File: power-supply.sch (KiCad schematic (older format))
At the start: 18 parts

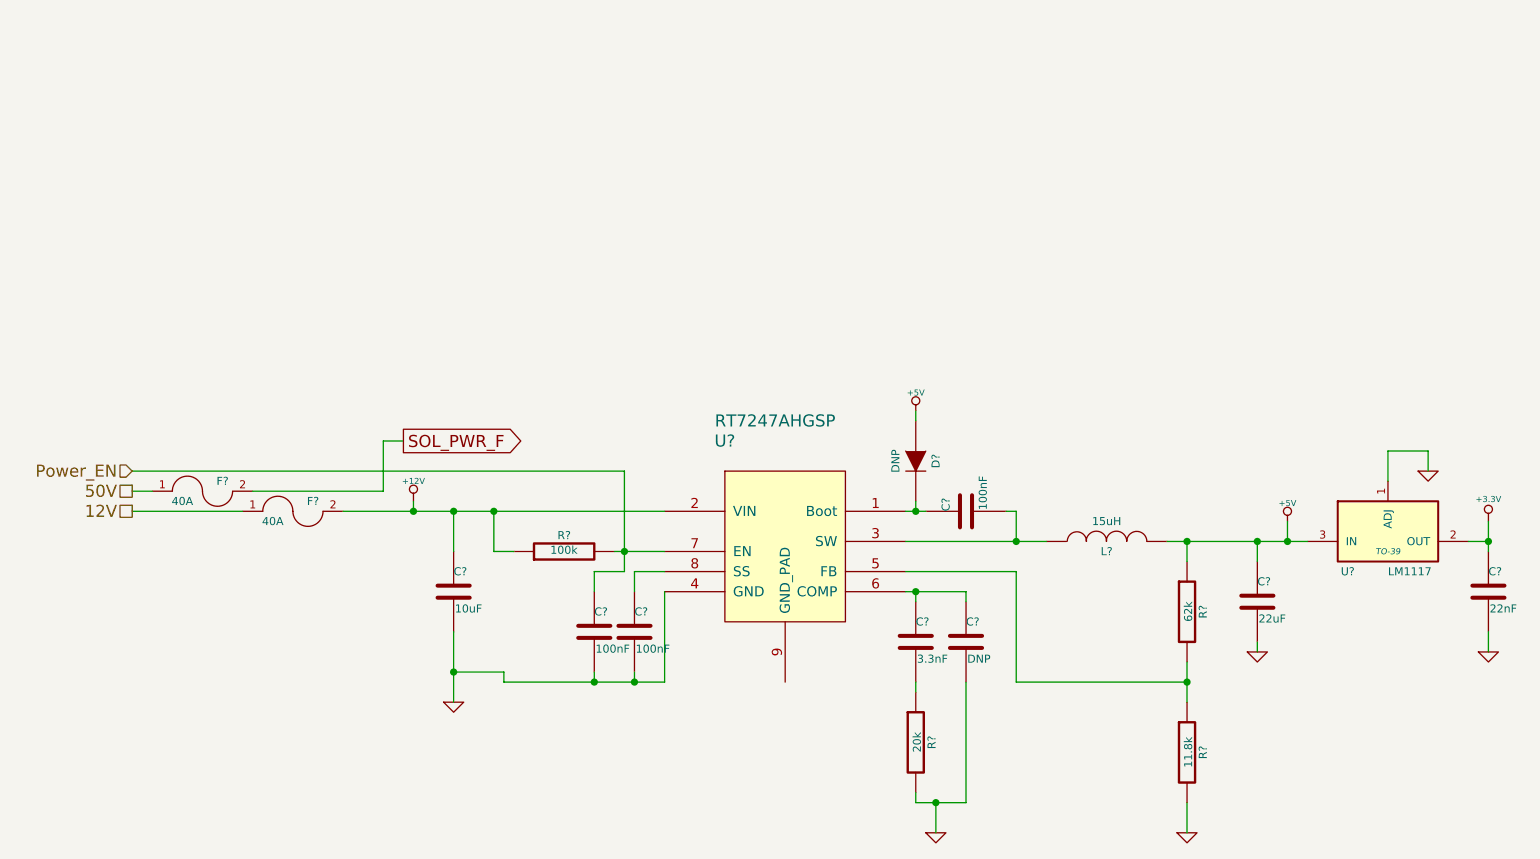
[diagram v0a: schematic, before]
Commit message: changed the controller adding some shift registers
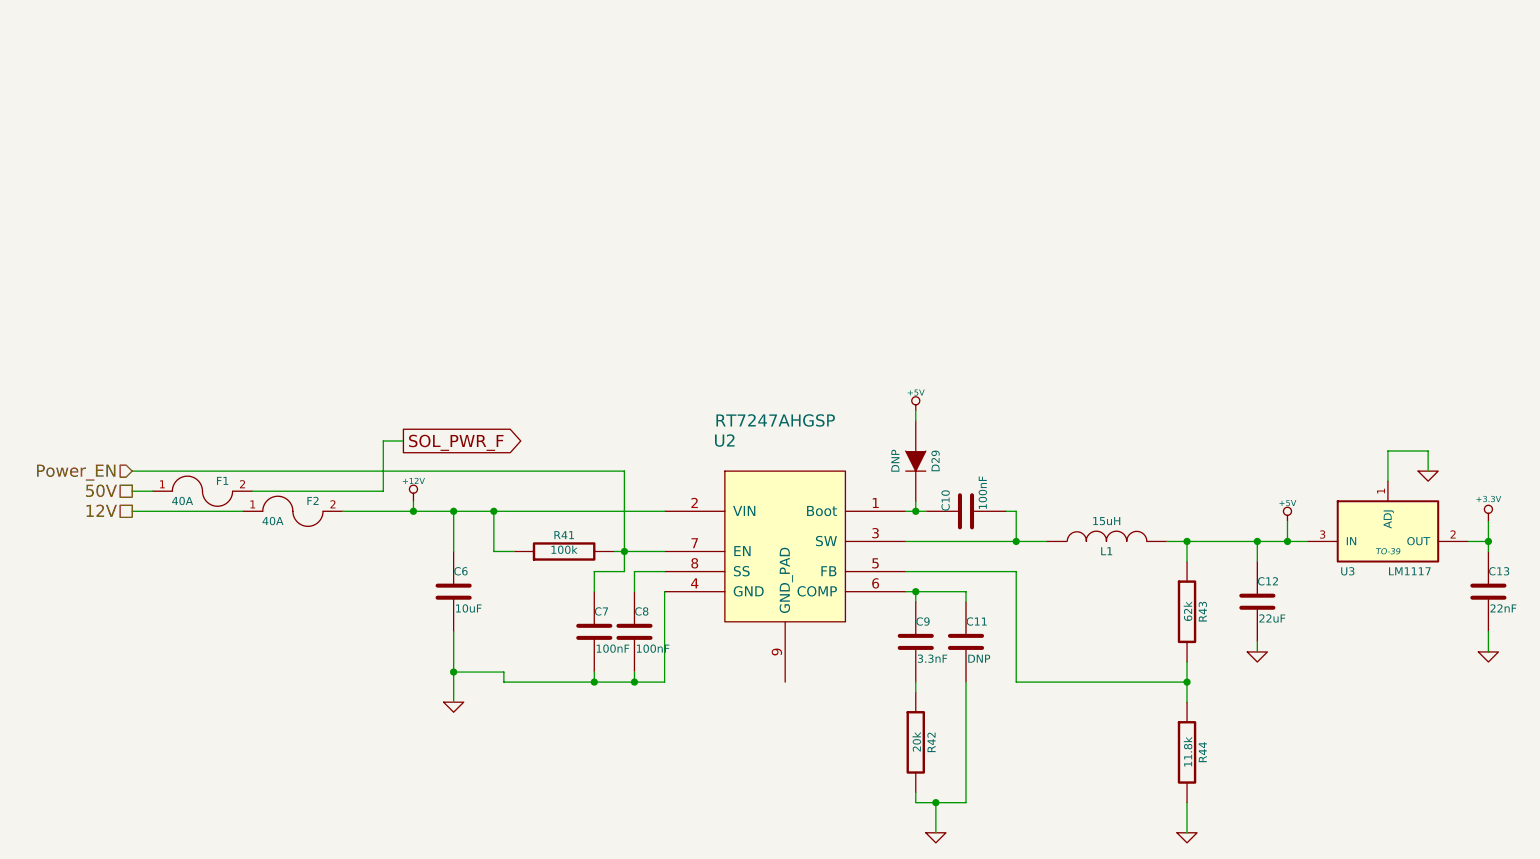
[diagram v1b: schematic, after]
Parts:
- gave numbers to parts that had none: 18
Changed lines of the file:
@@
-EESchema Schematic File Version 2  date 4/16/2013 9:07:53 PM
+EESchema Schematic File Version 2  date 4/17/2013 1:22:00 AM
 LIBS:power
 LIBS:device
@@
 LIBS:pinball-power
 LIBS:dips-s
+LIBS:Gajda_cmosieee
+LIBS:Gajda_ttlieee
 LIBS:base-module-cache
 EELAYER 27 0
@@
 $Descr A4 11693 8268
 encoding utf-8
-Sheet 6 10
+Sheet 5 10
 Title ""
 Date "17 apr 2013"
@@
 12V
 $Comp
-L C C?
+L C C6
 U 1 1 516B7ACF
 P 3000 3550
-F 0 "C?" H 3000 3650 40  0000 L CNN
+F 0 "C6" H 3000 3650 40  0000 L CNN
 F 1 "10uF" H 3006 3465 40  0000 L CNN
 F 2 "~" H 3038 3400 30  0000 C CNN
@@
 $EndComp
 $Comp
-L GND #PWR?
+L GND #PWR22
 U 1 1 516B7ADE
 P 3000 4100
-F 0 "#PWR?" H 3000 4100 30  0001 C CNN
+F 0 "#PWR22" H 3000 4100 30  0001 C CNN
 F 1 "GND" H 3000 4030 30  0001 C CNN
 F 2 "" H 3000 4100 60  0000 C CNN
@@
 $EndComp
 $Comp
-L C C?
+L C C8
 U 1 1 516B7AF4
 P 3900 3750
-F 0 "C?" H 3900 3850 40  0000 L CNN
+F 0 "C8" H 3900 3850 40  0000 L CNN
 F 1 "100nF" H 3906 3665 40  0000 L CNN
 F 2 "~" H 3938 3600 30  0000 C CNN
@@
 $EndComp
 $Comp
-L C C?
+L C C10
 U 1 1 516B7B0E
 P 5550 3150
-F 0 "C?" H 5550 3250 40  0000 L CNN
+F 0 "C10" H 5550 3250 40  0000 L CNN
 F 1 "100nF" H 5556 3065 40  0000 L CNN
 F 2 "~" H 5588 3000 30  0000 C CNN
@@
 $EndComp
 $Comp
-L INDUCTOR L?
+L INDUCTOR L1
 U 1 1 516B7B25
 P 6250 3300
-F 0 "L?" V 6200 3300 40  0000 C CNN
+F 0 "L1" V 6200 3300 40  0000 C CNN
 F 1 "15uH" V 6350 3300 40  0000 C CNN
 F 2 "~" H 6250 3300 60  0000 C CNN
@@
 $EndComp
 $Comp
-L R R?
+L R R43
 U 1 1 516B7B34
 P 6650 3650
-F 0 "R?" V 6730 3650 40  0000 C CNN
+F 0 "R43" V 6730 3650 40  0000 C CNN
 F 1 "62k" V 6657 3651 40  0000 C CNN
 F 2 "~" V 6580 3650 30  0000 C CNN
@@
 $EndComp
 $Comp
-L R R?
+L R R44
 U 1 1 516B7B41
 P 6650 4350
-F 0 "R?" V 6730 4350 40  0000 C CNN
+F 0 "R44" V 6730 4350 40  0000 C CNN
 F 1 "11.8k" V 6657 4351 40  0000 C CNN
 F 2 "~" V 6580 4350 30  0000 C CNN
@@
 $EndComp
 $Comp
-L C C?
+L C C9
 U 1 1 516B7B5B
 P 5300 3800
-F 0 "C?" H 5300 3900 40  0000 L CNN
+F 0 "C9" H 5300 3900 40  0000 L CNN
 F 1 "3.3nF" H 5306 3715 40  0000 L CNN
 F 2 "~" H 5338 3650 30  0000 C CNN
@@
 $EndComp
 $Comp
-L C C?
+L C C11
 U 1 1 516B7B61
 P 5550 3800
-F 0 "C?" H 5550 3900 40  0000 L CNN
+F 0 "C11" H 5550 3900 40  0000 L CNN
 F 1 "DNP" H 5556 3715 40  0000 L CNN
 F 2 "~" H 5588 3650 30  0000 C CNN
@@
 $EndComp
 $Comp
-L R R?
+L R R42
 U 1 1 516B7B67
 P 5300 4300
-F 0 "R?" V 5380 4300 40  0000 C CNN
+F 0 "R42" V 5380 4300 40  0000 C CNN
 F 1 "20k" V 5307 4301 40  0000 C CNN
 F 2 "~" V 5230 4300 30  0000 C CNN
@@
 $EndComp
 $Comp
-L GND #PWR?
+L GND #PWR24
 U 1 1 516B7CE2
 P 5400 4750
-F 0 "#PWR?" H 5400 4750 30  0001 C CNN
+F 0 "#PWR24" H 5400 4750 30  0001 C CNN
 F 1 "GND" H 5400 4680 30  0001 C CNN
 F 2 "" H 5400 4750 60  0000 C CNN
@@
 $EndComp
 $Comp
-L GND #PWR?
+L GND #PWR25
 U 1 1 516B7CE8
 P 6650 4750
-F 0 "#PWR?" H 6650 4750 30  0001 C CNN
+F 0 "#PWR25" H 6650 4750 30  0001 C CNN
 F 1 "GND" H 6650 4680 30  0001 C CNN
 F 2 "" H 6650 4750 60  0000 C CNN
@@
 $EndComp
 $Comp
-L C C?
+L C C12
 U 1 1 516B7D79
 P 7000 3600
-F 0 "C?" H 7000 3700 40  0000 L CNN
+F 0 "C12" H 7000 3700 40  0000 L CNN
 F 1 "22uF" H 7006 3515 40  0000 L CNN
 F 2 "~" H 7038 3450 30  0000 C CNN
@@
 $EndComp
 $Comp
-L GND #PWR?
+L GND #PWR26
 U 1 1 516B7DE8
 P 7000 3850
-F 0 "#PWR?" H 7000 3850 30  0001 C CNN
+F 0 "#PWR26" H 7000 3850 30  0001 C CNN
 F 1 "GND" H 7000 3780 30  0001 C CNN
 F 2 "" H 7000 3850 60  0000 C CNN
@@
 $EndComp
 $Comp
-L +5V #PWR?
+L +5V #PWR27
 U 1 1 516B7E14
 P 7150 3200
-F 0 "#PWR?" H 7150 3290 20  0001 C CNN
+F 0 "#PWR27" H 7150 3290 20  0001 C CNN
 F 1 "+5V" H 7150 3290 30  0000 C CNN
 F 2 "" H 7150 3200 60  0000 C CNN
@@
 $EndComp
 $Comp
-L LM137H U?
+L LM137H U3
 U 1 1 516B7E76
 P 7650 3250
-F 0 "U?" H 7450 3050 40  0000 C CNN
+F 0 "U3" H 7450 3050 40  0000 C CNN
 F 1 "LM1117" H 7650 3050 40  0000 L CNN
 F 2 "TO-39" H 7650 3150 30  0000 C CIN
@@
 $EndComp
 $Comp
-L GND #PWR?
+L GND #PWR28
 U 1 1 516B7EDB
 P 7850 2950
-F 0 "#PWR?" H 7850 2950 30  0001 C CNN
+F 0 "#PWR28" H 7850 2950 30  0001 C CNN
 F 1 "GND" H 7850 2880 30  0001 C CNN
 F 2 "" H 7850 2950 60  0000 C CNN
@@
 $EndComp
 $Comp
-L +3.3V #PWR?
+L +3.3V #PWR29
 U 1 1 516B7F0C
 P 8150 3200
-F 0 "#PWR?" H 8150 3160 30  0001 C CNN
+F 0 "#PWR29" H 8150 3160 30  0001 C CNN
 F 1 "+3.3V" H 8150 3310 30  0000 C CNN
 F 2 "" H 8150 3200 60  0000 C CNN
@@
 $EndComp
 $Comp
-L C C?
+L C C13
 U 1 1 516B7F44
 P 8150 3550
-F 0 "C?" H 8150 3650 40  0000 L CNN
+F 0 "C13" H 8150 3650 40  0000 L CNN
 F 1 "22nF" H 8156 3465 40  0000 L CNN
 F 2 "~" H 8188 3400 30  0000 C CNN
@@
 $EndComp
 $Comp
-L GND #PWR?
+L GND #PWR30
 U 1 1 516B7F4A
 P 8150 3850
-F 0 "#PWR?" H 8150 3850 30  0001 C CNN
+F 0 "#PWR30" H 8150 3850 30  0001 C CNN
 F 1 "GND" H 8150 3780 30  0001 C CNN
 F 2 "" H 8150 3850 60  0000 C CNN
@@
 $EndComp
 $Comp
-L R R?
+L R R41
 U 1 1 516B81BC
 P 3550 3350
-F 0 "R?" V 3630 3350 40  0000 C CNN
+F 0 "R41" V 3630 3350 40  0000 C CNN
 F 1 "100k" V 3557 3351 40  0000 C CNN
 F 2 "~" V 3480 3350 30  0000 C CNN
@@
 $EndComp
 $Comp
-L DIODE D?
+L DIODE D29
 U 1 1 516B8761
 P 5300 2900
-F 0 "D?" H 5300 3000 40  0000 C CNN
+F 0 "D29" H 5300 3000 40  0000 C CNN
 F 1 "DNP" H 5300 2800 40  0000 C CNN
 F 2 "~" H 5300 2900 60  0000 C CNN
@@
 $EndComp
 $Comp
-L +5V #PWR?
+L +5V #PWR23
 U 1 1 516B87A2
 P 5300 2650
-F 0 "#PWR?" H 5300 2740 20  0001 C CNN
+F 0 "#PWR23" H 5300 2740 20  0001 C CNN
 F 1 "+5V" H 5300 2740 30  0000 C CNN
 F 2 "" H 5300 2650 60  0000 C CNN
@@
 $EndComp
 $Comp
-L C C?
+L C C7
 U 1 1 516B8BF3
 P 3700 3750
-F 0 "C?" H 3700 3850 40  0000 L CNN
+F 0 "C7" H 3700 3850 40  0000 L CNN
 F 1 "100nF" H 3706 3665 40  0000 L CNN
 F 2 "~" H 3738 3600 30  0000 C CNN
@@
 SOL_PWR_F
 $Comp
-L FUSE F?
+L FUSE F1
 U 1 1 516D27EC
 P 1750 3050
-F 0 "F?" H 1850 3100 40  0000 C CNN
+F 0 "F1" H 1850 3100 40  0000 C CNN
 F 1 "40A" H 1650 3000 40  0000 C CNN
 F 2 "~" H 1750 3050 60  0000 C CNN
@@
 $EndComp
 $Comp
-L FUSE F?
+L FUSE F2
 U 1 1 516D2839
 P 2200 3150
-F 0 "F?" H 2300 3200 40  0000 C CNN
+F 0 "F2" H 2300 3200 40  0000 C CNN
 F 1 "40A" H 2100 3100 40  0000 C CNN
 F 2 "~" H 2200 3150 60  0000 C CNN
@@
 $EndComp
 $Comp
-L RT7247AHGSP U?
+L RT7247AHGSP U2
 U 1 1 516D4B84
 P 4600 3350
-F 0 "U?" H 4350 3900 60  0000 C CNN
+F 0 "U2" H 4350 3900 60  0000 C CNN
 F 1 "RT7247AHGSP" H 4600 4000 60  0000 C CNN
 F 2 "~" H 4600 3350 60  0000 C CNN
@@
 $EndComp
 $Comp
-L +12V #PWR?
+L +12V #PWR21
 U 1 1 516D7A31
 P 2800 3100
-F 0 "#PWR?" H 2800 3050 20  0001 C CNN
+F 0 "#PWR21" H 2800 3050 20  0001 C CNN
 F 1 "+12V" H 2800 3200 30  0000 C CNN
 F 2 "" H 2800 3100 60  0000 C CNN

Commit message: finished main controller, added LED's to power system.
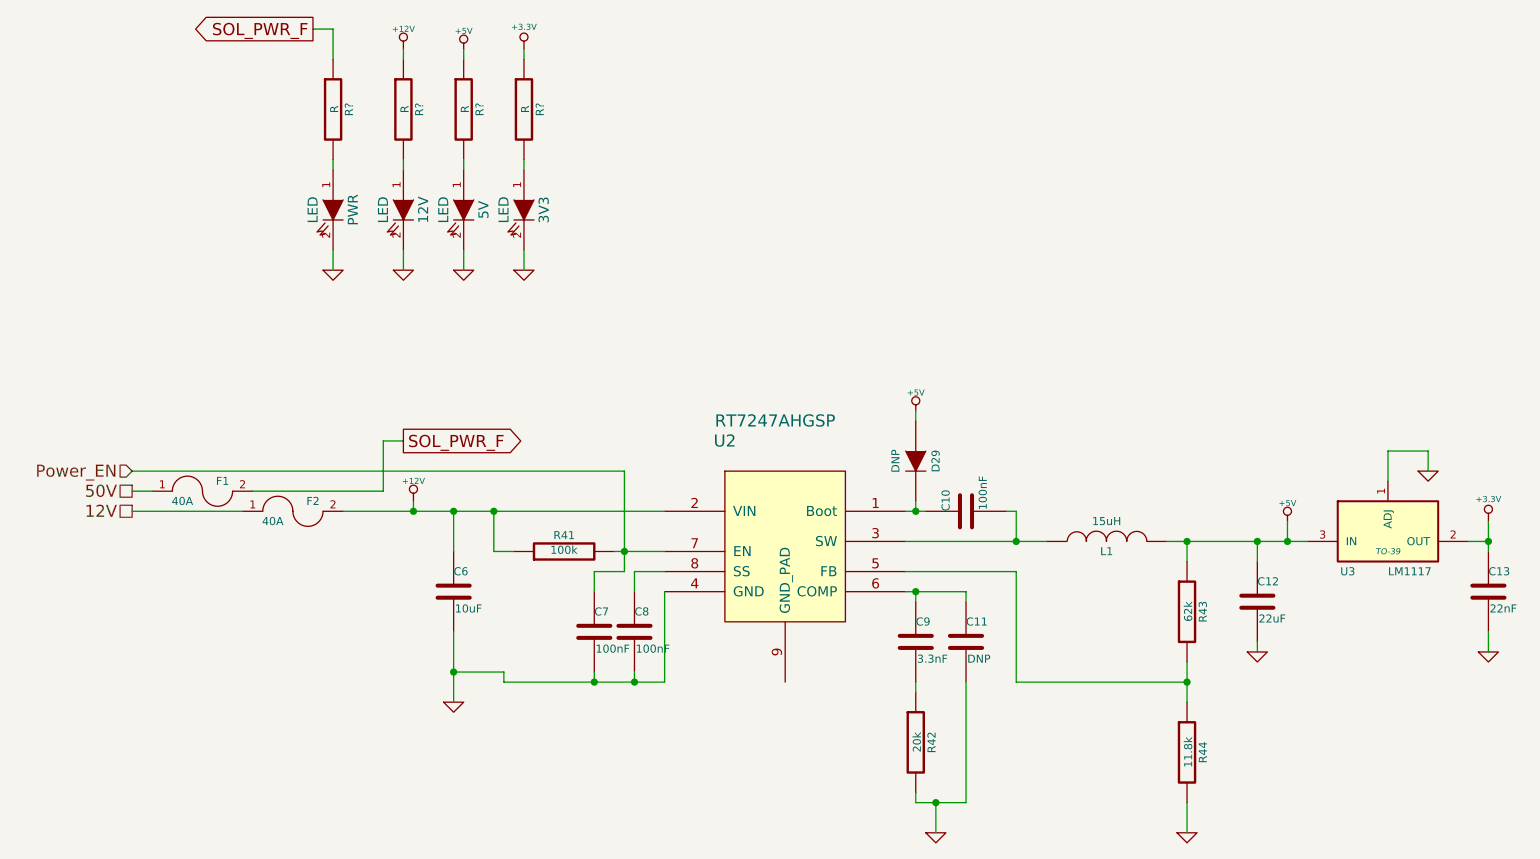
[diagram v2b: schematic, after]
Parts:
- added 12V, 3V3, 5V, PWR: LED, ~, symbol LED
- added R? (x4): R, ~, symbol R
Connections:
- net +12V: now also R?.1
- net +3.3V: now also R?.1
- net +5V: now also R?.1
- net GND: now also 12V.2 (K), 3V3.2 (K), 5V.2 (K), PWR.2 (K)
- net SOL_PWR_F: now also R?.1
- new net: PWR.1 (A), R?.2
- new net: 12V.1 (A), R?.2
- new net: 5V.1 (A), R?.2
- new net: 3V3.1 (A), R?.2
